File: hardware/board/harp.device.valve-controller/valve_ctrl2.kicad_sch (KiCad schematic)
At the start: 52 parts, among them J1 Screw_Terminal_01x02, J10 Screw_Terminal_01x02, J11 Screw_Terminal_01x02, J14 Screw_Terminal_01x02, J3 Screw_Terminal_01x02, J6 Screw_Terminal_01x02, J7 Screw_Terminal_01x02, J9 Screw_Terminal_01x02, Q1 CSD17570Q5B, Q10 CSD17570Q5B, Q3 CSD17570Q5B, Q4 CSD17570Q5B, Q5 CSD17570Q5B, Q6 CSD17570Q5B, Q7 CSD17570Q5B, Q8 CSD17570Q5B, U1 MIC4127, U10 MIC4127, U6 MIC4127, U8 MIC4127

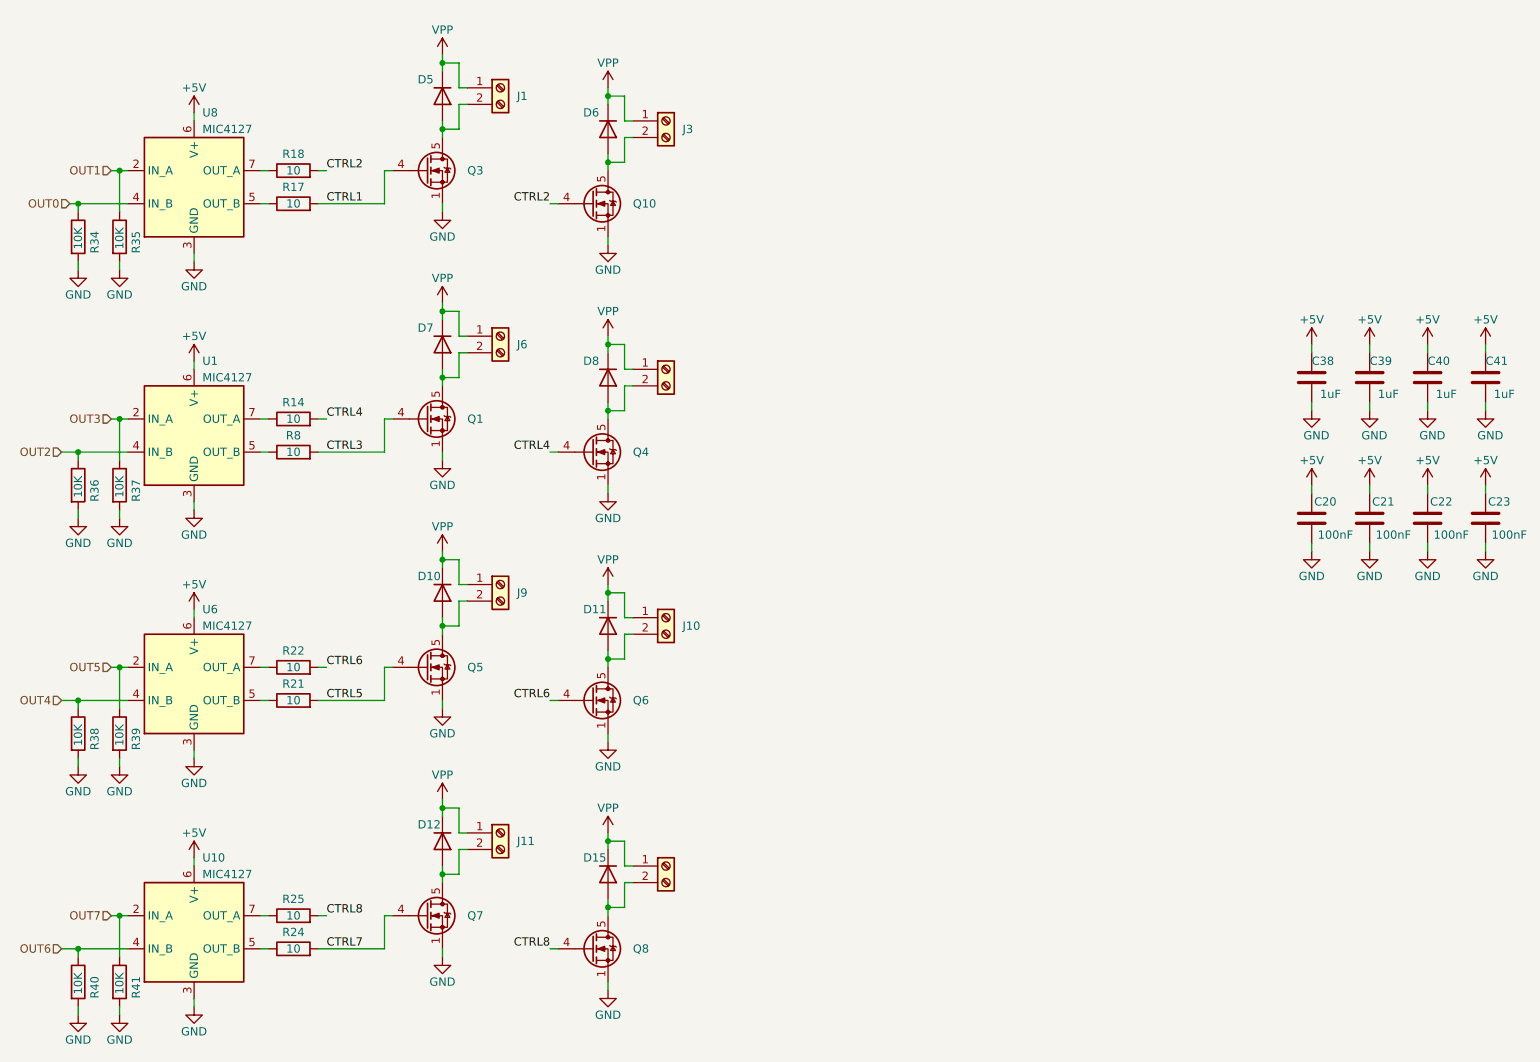
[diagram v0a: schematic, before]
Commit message: update pcb power supply
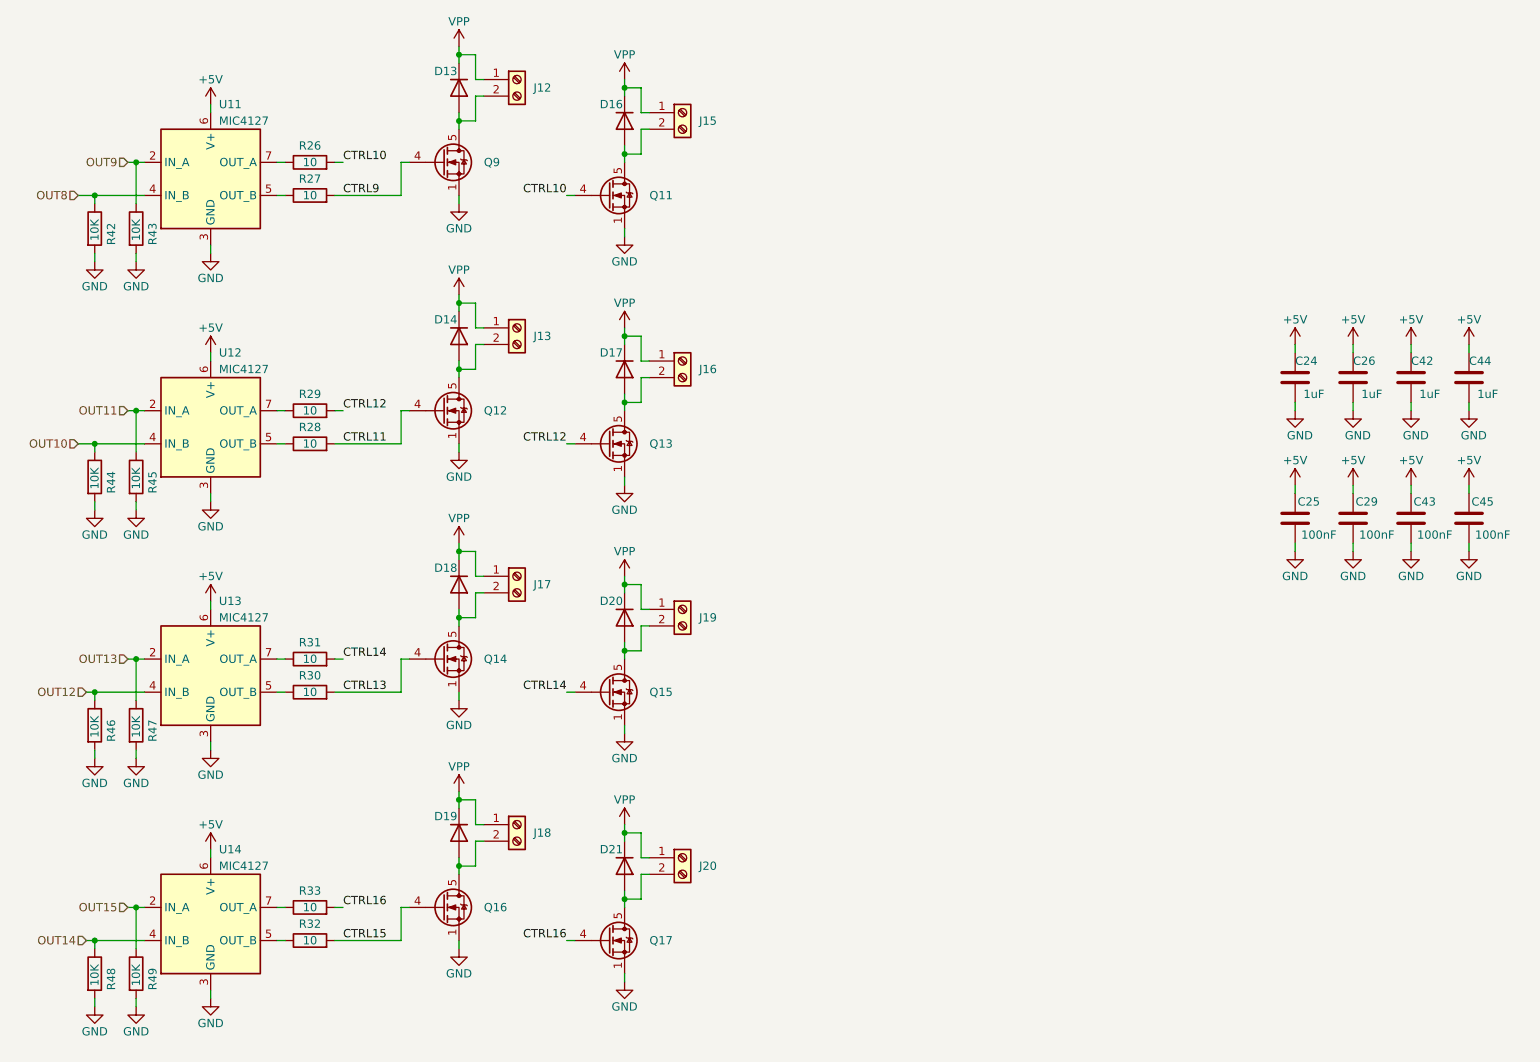
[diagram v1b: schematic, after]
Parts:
- removed C20, C21, C22, C23: 100nF, Capacitor_SMD:C_0402_1005Metric, symbol Device:C
- removed C38, C39, C40, C41: 1uF, Capacitor_SMD:C_0402_1005Metric, symbol Device:C
- removed D10, D11, D12, D15, D5, D6, D7, D8: 1N4007FL, Diode_SMD:D_SOD-123F, symbol Device:D
- removed J1, J10, J11, J14, J3, J6, J7, J9: Screw_Terminal_01x02, Connector_Phoenix_MC:PhoenixContact_MC_1,5_2-G-3.5_1x02_P3.50mm_Horizontal, symbol Connector:Screw_Terminal_01x02
- removed Q1, Q10, Q3, Q4, Q5, Q6, Q7, Q8: CSD17570Q5B, Package_TO_SOT_SMD:TDSON-8-1, symbol Transistor_FET:CSD17570Q5B
- removed R14, R17, R18, R21, R22, R24, R25, R8: 10, Resistor_SMD:R_0603_1608Metric, symbol Device:R
- removed R34, R35, R36, R37, R38, R39, R40, R41: 10K, Resistor_SMD:R_0402_1005Metric, symbol Device:R
- removed U1, U10, U6, U8: MIC4127, Package_SO:MSOP-8-1EP_3x3mm_P0.65mm_EP1.5x1.8mm, symbol kicad-lib:MIC4127
- added C24, C26, C42, C44: 1uF, Capacitor_SMD:C_0402_1005Metric, symbol Device:C
- added C25, C29, C43, C45: 100nF, Capacitor_SMD:C_0402_1005Metric, symbol Device:C
- added D13, D14, D16, D17, D18, D19, D20, D21: 1N4007FL, Diode_SMD:D_SOD-123F, symbol Device:D
- added J12, J13, J15, J16, J17, J18, J19, J20: Screw_Terminal_01x02, Connector_Phoenix_MC:PhoenixContact_MC_1,5_2-G-3.5_1x02_P3.50mm_Horizontal, symbol Connector:Screw_Terminal_01x02
- added Q11, Q12, Q13, Q14, Q15, Q16, Q17, Q9: CSD17570Q5B, Package_TO_SOT_SMD:TDSON-8-1, symbol Transistor_FET:CSD17570Q5B
- added R26, R27, R28, R29, R30, R31, R32, R33: 10, Resistor_SMD:R_0603_1608Metric, symbol Device:R
- added R42, R43, R44, R45, R46, R47, R48, R49: 10K, Resistor_SMD:R_0402_1005Metric, symbol Device:R
- added U11, U12, U13, U14: MIC4127, Package_SO:MSOP-8-1EP_3x3mm_P0.65mm_EP1.5x1.8mm, symbol kicad-lib:MIC4127
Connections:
- net +5V: now also C24.1, C25.2, C26.1, C29.2, C42.1, C43.2, C44.1, C45.2, U11.6 (V+), U12.6 (V+), U13.6 (V+), U14.6 (V+)
- net GND: now also C24.2, C25.1, C26.2, C29.1, C42.2, C43.1, C44.2, C45.1, Q11.1 (S), Q11.2 (S), Q11.3 (S), Q12.1 (S), Q12.2 (S), Q12.3 (S), Q13.1 (S), Q13.2 (S), Q13.3 (S), Q14.1 (S), Q14.2 (S), Q14.3 (S), Q15.1 (S), Q15.2 (S), Q15.3 (S), Q16.1 (S), Q16.2 (S), Q16.3 (S), Q17.1 (S), Q17.2 (S), Q17.3 (S), Q9.1 (S), Q9.2 (S), Q9.3 (S), R42.2, R43.2, R44.2, R45.2, R46.2, R47.2, R48.2, R49.2, U11.3 (GND), U11.9 (GND), U12.3 (GND), U12.9 (GND), U13.3 (GND), U13.9 (GND), U14.3 (GND), U14.9 (GND)
- net VPP: now also D13.1 (K), D14.1 (K), D16.1 (K), D17.1 (K), D18.1 (K), D19.1 (K), D20.1 (K), D21.1 (K), J12.1 (Pin_1), J13.1 (Pin_1), J15.1 (Pin_1), J16.1 (Pin_1), J17.1 (Pin_1), J18.1 (Pin_1), J19.1 (Pin_1), J20.1 (Pin_1)
- new net: R32.1, U14.5 (OUT_B)
- new net: R33.1, U14.7 (OUT_A)
- new net: D21.2 (A), J20.2 (Pin_2), Q17.5 (D)
- new net: D18.2 (A), J17.2 (Pin_2), Q14.5 (D)
- new net: R28.1, U12.5 (OUT_B)
- new net: D14.2 (A), J13.2 (Pin_2), Q12.5 (D)
- new net: R29.1, U12.7 (OUT_A)
- new net: R31.1, U13.7 (OUT_A)
- new net: D19.2 (A), J18.2 (Pin_2), Q16.5 (D)
- new net: D16.2 (A), J15.2 (Pin_2), Q11.5 (D)
- new net: R27.1, U11.5 (OUT_B)
- new net: D17.2 (A), J16.2 (Pin_2), Q13.5 (D)
- new net: D20.2 (A), J19.2 (Pin_2), Q15.5 (D)
- new net: D13.2 (A), J12.2 (Pin_2), Q9.5 (D)
- new net: R30.1, U13.5 (OUT_B)
- new net: R26.1, U11.7 (OUT_A)
- new net CTRL10: Q11.4 (G), R26.2
- new net CTRL11: Q12.4 (G), R28.2
- new net CTRL12: Q13.4 (G), R29.2
- new net CTRL13: Q14.4 (G), R30.2
- new net CTRL14: Q15.4 (G), R31.2
- new net CTRL15: Q16.4 (G), R32.2
- new net CTRL16: Q17.4 (G), R33.2
- new net CTRL9: Q9.4 (G), R27.2
- new net OUT10: R44.1, U12.4 (IN_B)
- new net OUT11: R45.1, U12.2 (IN_A)
- new net OUT12: R46.1, U13.4 (IN_B)
- new net OUT13: R47.1, U13.2 (IN_A)
- new net OUT14: R48.1, U14.4 (IN_B)
- new net OUT15: R49.1, U14.2 (IN_A)
- new net OUT8: R42.1, U11.4 (IN_B)
- new net OUT9: R43.1, U11.2 (IN_A)

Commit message: update bom
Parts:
- J12, J13, J15, J16, J17, J18, J19, J20: Manufacturer (none) -> Phoenix Contact; Manufacturer Number (none) -> 1844210; Notes (none) -> mates with Phoenix Contact 1840366
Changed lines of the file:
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@@
 			)
 		)
-		(property "Datasheet" "~"
+		(property "Datasheet" "https://www.phoenixcontact.com/en-us/products/pcb-header-mc-15-2-g-35-1844210?type=pdf"
 			(at 127 67.31 0)
 			(effects
@@
 			)
 		)
+		(property "Manufacturer" "Phoenix Contact"
+			(at 127 67.31 0)
+			(effects
+				(font
+					(size 1.27 1.27)
+				)
+				(hide yes)
+			)
+		)
+		(property "Manufacturer Number" "1844210"
+			(at 127 67.31 0)
+			(effects
+				(font
+					(size 1.27 1.27)
+				)
+				(hide yes)
+			)
+		)
+		(property "Notes" "mates with Phoenix Contact 1840366"
+			(at 127 67.31 0)
+			(effects
+				(font
+					(size 1.27 1.27)
+				)
+				(hide yes)
+			)
+		)
 		(pin "2"
 		)
@@
 			)
 		)
-		(property "Datasheet" "~"
+		(property "Datasheet" "https://www.phoenixcontact.com/en-us/products/pcb-header-mc-15-2-g-35-1844210?type=pdf"
 			(at 152.4 148.59 0)
 			(effects
@@
 			)
 		)
+		(property "Manufacturer" "Phoenix Contact"
+			(at 152.4 148.59 0)
+			(effects
+				(font
+					(size 1.27 1.27)
+				)
+				(hide yes)
+			)
+		)
+		(property "Manufacturer Number" "1844210"
+			(at 152.4 148.59 0)
+			(effects
+				(font
+					(size 1.27 1.27)
+				)
+				(hide yes)
+			)
+		)
+		(property "Notes" "mates with Phoenix Contact 1840366"
+			(at 152.4 148.59 0)
+			(effects
+				(font
+					(size 1.27 1.27)
+				)
+				(hide yes)
+			)
+		)
 		(pin "2"
 		)
@@
 			)
 		)
-		(property "Datasheet" "~"
+		(property "Datasheet" "https://www.phoenixcontact.com/en-us/products/pcb-header-mc-15-2-g-35-1844210?type=pdf"
 			(at 152.4 34.29 0)
 			(effects
@@
 			)
 		)
+		(property "Manufacturer" "Phoenix Contact"
+			(at 152.4 34.29 0)
+			(effects
+				(font
+					(size 1.27 1.27)
+				)
+				(hide yes)
+			)
+		)
+		(property "Manufacturer Number" "1844210"
+			(at 152.4 34.29 0)
+			(effects
+				(font
+					(size 1.27 1.27)
+				)
+				(hide yes)
+			)
+		)
+		(property "Notes" "mates with Phoenix Contact 1840366"
+			(at 152.4 34.29 0)
+			(effects
+				(font
+					(size 1.27 1.27)
+				)
+				(hide yes)
+			)
+		)
 		(pin "2"
 		)
@@
 			)
 		)
-		(property "Datasheet" "~"
+		(property "Datasheet" "https://www.phoenixcontact.com/en-us/products/pcb-header-mc-15-2-g-35-1844210?type=pdf"
 			(at 152.4 72.39 0)
 			(effects
@@
 			)
 		)
+		(property "Manufacturer" "Phoenix Contact"
+			(at 152.4 72.39 0)
+			(effects
+				(font
+					(size 1.27 1.27)
+				)
+				(hide yes)
+			)
+		)
+		(property "Manufacturer Number" "1844210"
+			(at 152.4 72.39 0)
+			(effects
+				(font
+					(size 1.27 1.27)
+				)
+				(hide yes)
+			)
+		)
+		(property "Notes" "mates with Phoenix Contact 1840366"
+			(at 152.4 72.39 0)
+			(effects
+				(font
+					(size 1.27 1.27)
+				)
+				(hide yes)
+			)
+		)
 		(pin "2"
 		)
@@
 			)
 		)
-		(property "Datasheet" "~"
+		(property "Datasheet" "https://www.phoenixcontact.com/en-us/products/pcb-header-mc-15-2-g-35-1844210?type=pdf"
 			(at 127 105.41 0)
 			(effects
@@
 			)
 		)
+		(property "Manufacturer" "Phoenix Contact"
+			(at 127 105.41 0)
+			(effects
+				(font
+					(size 1.27 1.27)
+				)
+				(hide yes)
+			)
+		)
+		(property "Manufacturer Number" "1844210"
+			(at 127 105.41 0)
+			(effects
+				(font
+					(size 1.27 1.27)
+				)
+				(hide yes)
+			)
+		)
+		(property "Notes" "mates with Phoenix Contact 1840366"
+			(at 127 105.41 0)
+			(effects
+				(font
+					(size 1.27 1.27)
+				)
+				(hide yes)
+			)
+		)
 		(pin "2"
 		)
@@
 			)
 		)
-		(property "Datasheet" "~"
+		(property "Datasheet" "https://www.phoenixcontact.com/en-us/products/pcb-header-mc-15-2-g-35-1844210?type=pdf"
 			(at 127 143.51 0)
 			(effects
@@
 			)
 		)
+		(property "Manufacturer" "Phoenix Contact"
+			(at 127 143.51 0)
+			(effects
+				(font
+					(size 1.27 1.27)
+				)
+				(hide yes)
+			)
+		)
+		(property "Manufacturer Number" "1844210"
+			(at 127 143.51 0)
+			(effects
+				(font
+					(size 1.27 1.27)
+				)
+				(hide yes)
+			)
+		)
+		(property "Notes" "mates with Phoenix Contact 1840366"
+			(at 127 143.51 0)
+			(effects
+				(font
+					(size 1.27 1.27)
+				)
+				(hide yes)
+			)
+		)
 		(pin "2"
 		)
@@
 			)
 		)
-		(property "Datasheet" "~"
+		(property "Datasheet" "https://www.phoenixcontact.com/en-us/products/pcb-header-mc-15-2-g-35-1844210?type=pdf"
 			(at 127 29.21 0)
 			(effects
@@
 			)
 		)
+		(property "Manufacturer" "Phoenix Contact"
+			(at 127 29.21 0)
+			(effects
+				(font
+					(size 1.27 1.27)
+				)
+				(hide yes)
+			)
+		)
+		(property "Manufacturer Number" "1844210"
+			(at 127 29.21 0)
+			(effects
+				(font
+					(size 1.27 1.27)
+				)
+				(hide yes)
+			)
+		)
+		(property "Notes" "mates with Phoenix Contact 1840366"
+			(at 127 29.21 0)
+			(effects
+				(font
+					(size 1.27 1.27)
+				)
+				(hide yes)
+			)
+		)
 		(pin "2"
 		)
@@
 			)
 		)
-		(property "Datasheet" "~"
+		(property "Datasheet" "https://www.phoenixcontact.com/en-us/products/pcb-header-mc-15-2-g-35-1844210?type=pdf"
 			(at 152.4 110.49 0)
 			(effects
@@
 			(at 152.4 110.49 0)
 			(effects
+				(font
+					(size 1.27 1.27)
+				)
+				(hide yes)
+			)
+		)
+		(property "Manufacturer" "Phoenix Contact"
+			(at 152.4 110.49 0)
+			(effects
+				(font
+					(size 1.27 1.27)
+				)
+				(hide yes)
+			)
+		)
+		(property "Manufacturer Number" "1844210"
+			(at 152.4 110.49 0)
+			(effects
+				(font
+					(size 1.27 1.27)
+				)
+				(hide yes)
+			)
+		)
+		(property "Notes" "mates with Phoenix Contact 1840366"
+			(at 152.4 110.49 0)
+			(effects

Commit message: prep hw initial release
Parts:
- C25, C29, C43, C45: Link https://www.digikey.com/en/products/detail/walsin-technolog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 -> https://www.digikey.com/en/products/detail/murata-electroni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; Manufacturer Walson Technology Corporation -> Murata Electronics; Manufacturer Number 0402B104K160CT -> GRM155R71H104KE14D; Rated Voltage 16V -> 50V
- Q11, Q12, Q13, Q14, Q15, Q16, Q17, Q9: Link (none) -> https://www.digikey.com/en/products/detail/texas-instrument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; Manufacturer (none) -> Texas Instruments; Manufacturer Number (none) -> CSD17570Q5B
- R26, R27, R28, R29, R30, R31, R32, R33: Link (none) -> https://www.digikey.com/en/products/detail/vishay-dale/RCA0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; Manufacturer (none) -> Vishay Dale; Manufacturer Number (none) -> RCA060310R0FKEAHP; Notes (none) -> 1/3W; Tolerance (none) -> 1%
- U11, U12, U13, U14: Manufacturer (none) -> Microchip Technology
